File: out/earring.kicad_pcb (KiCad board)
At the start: 4 copper layers, 30.5 x 35.8 mm, 123 parts, among them J1 USB-C, SW1 BOOTSEL, SW2 PWR, U1 RP2350A, U2 LGS4056H, U3 NCP730-3.3, U4 TPS22913, U5 USBLC6-2P6, U6 LSM6DS3TR-C, U7 W25Q16JVUXIQ, Y1 12MHz

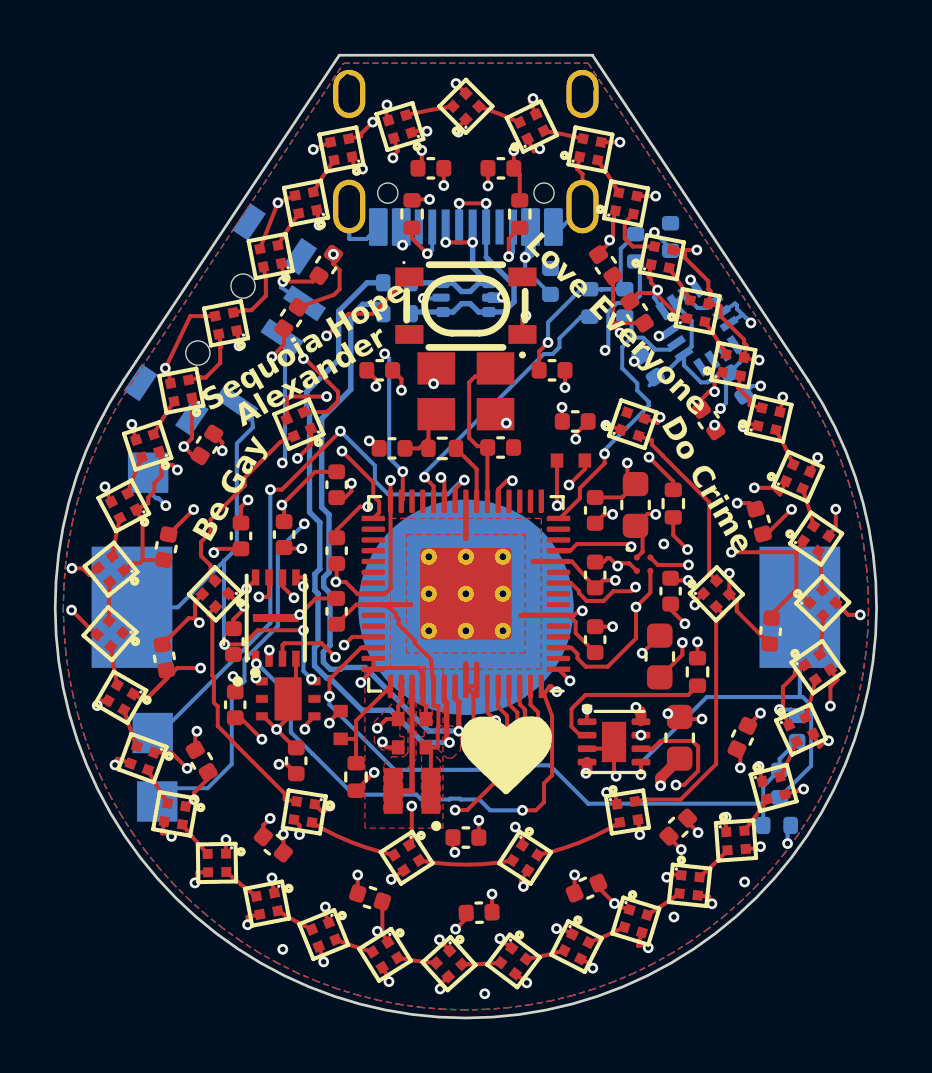
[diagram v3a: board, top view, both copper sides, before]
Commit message: Rev 2 power path: split VBATT from VSYS so USB runs the board
Rev 1 hung the LDO input and the LED load switch on VBATT -- the same
node as the charger's BAT pin -- so the LGS4056H's ~41mA program current
was SHARED with the running system. 17mA of MCU plus 17.5mA of LED rail
left the cell about 6mA, and a flat cell could never climb to the
SK6805-EC10's 3.7V minimum VDD before someone unplugged it. That is the
"no lights at all" failure from Aug 27, and it is a power-path problem,
not a firmware one.

  VBUS  --|>|--  VSYS      D3, B5819WS Schottky, ~0.3V at our ~60mA
  VBATT --[Q2]-- VSYS      CJ2101 P-FET, on only when no cable is in
  VSYS  -> U3 (LDO IN), U4 (LED load switch IN), C18, C29
  VBATT -> U2 pin 5 (charger BAT), BT1, C17, SW2   [cell node ONLY]

Q2's ORIENTATION IS THE WHOLE TRICK: source = VSYS, drain = VBATT. A
P-FET's body diode conducts drain->source, so this way it points
cell->VSYS. It blocks the 4.7V USB rail from back-feeding the cell
around the charger -- which is exactly what the intuitive wiring
(source on the battery) would do through the body diode -- while still
letting the cell carry the load through ~0.4V of diode if VSYS sags
below VBATT, covering the ~200ms of VBUS decay on unplug. Gate is
R22 10k from VBUS against R21 1M to GND: near VBUS with a cable in
(Vgs +0.25V, hard off), and following the dead VBUS node without one.
That node is not floating -- R19/R20 pin it under 0.65V even against
R18's backfeed -- so Vgs is -2.4V at a 3.0V cell and Q2 is fully on.

This retires the R8 22k->15k rework rather than performing it. 22k
already gives 40.9mA, which is exactly the fitted RJD2032C1's rated
40mA charge, and the reason 15k was tempting is gone. The hazard that
blocked it is gone too: with the system off the cell, the full program
current reaches the cell in EITHER switch position.

What else falls out: DONE can finally assert (the cell's current
actually tapers to ITERM now), VBSENSE reads a true unloaded cell while
charging, the r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
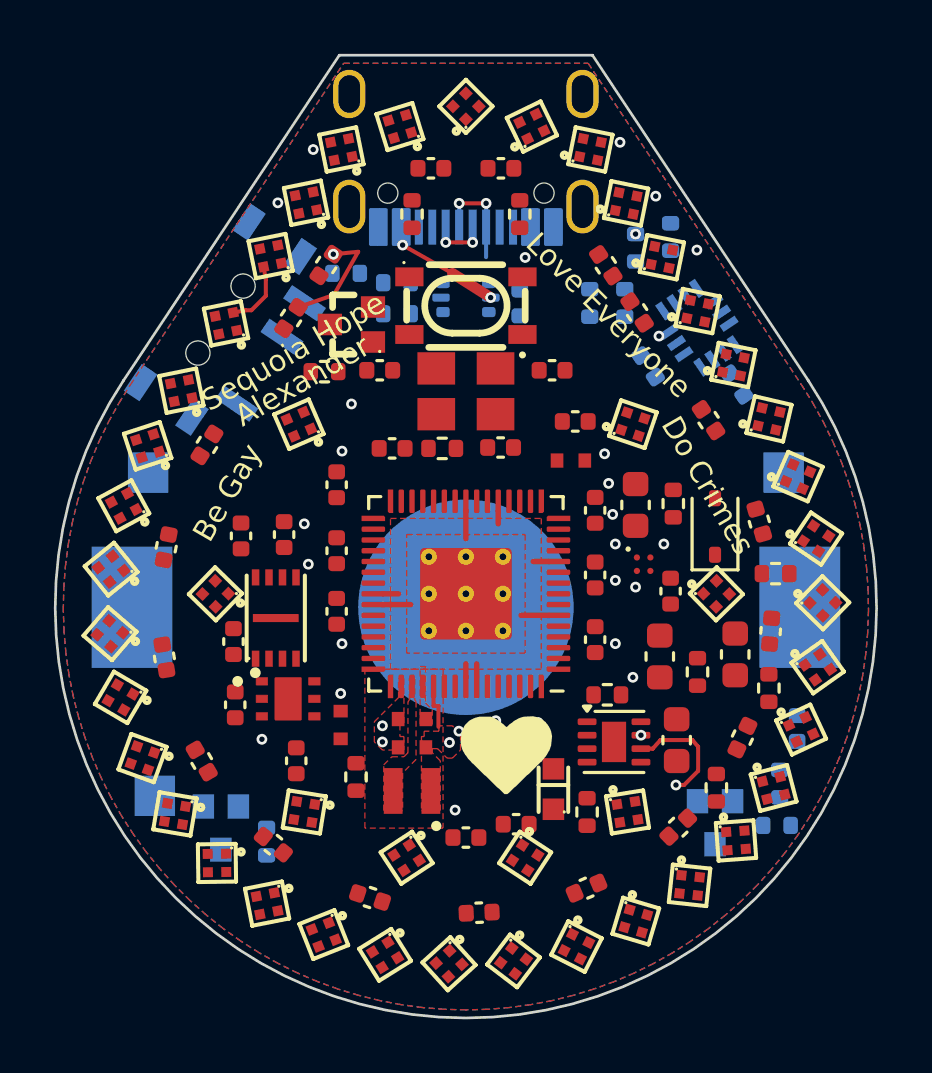
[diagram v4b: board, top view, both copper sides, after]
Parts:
- added C26: 100n, earring:C_0402_1005Metric, F.Cu at (101.9, 108.1)
- added C29: 10u, earring:C_0603_1608Metric, F.Cu at (110.0, 101.8)
- added D2: BAT54S, earring:SOT-323_BAT54SW, B.Cu at (90.9, 108.2)
- added D3: B5819WS, earring:D_SOD-323, F.Cu at (109.2, 97.0)
- added Q1: ALS-PT19, earring:SENSOR_ALS-PT19, F.Cu at (103.2, 106.8)
- added Q2: CJ2101, earring:SOT-323_MOSFET, B.Cu at (109.2, 108.0)
- added Q3: BSS138W, earring:SOT-323_MOSFET, F.Cu at (95.8, 89.5)
- added R16: 22k, earring:R_0402_1005Metric, F.Cu at (104.5, 107.6)
- added R17: 100k, earring:R_0402_1005Metric, B.Cu at (92.6, 108.7)
- added R18: 100k, earring:R_0402_1005Metric, B.Cu at (95.5, 87.6)
- added R19: 10k, earring:R_0402_1005Metric, F.Cu at (105.2, 103.2)
- added R20: 10k, earring:R_0402_1005Metric, F.Cu at (111.5, 98.8)
- added R21: 1M, earring:R_0402_1005Metric, F.Cu at (111.2, 103.0)
- added R22: 10k, earring:R_0402_1005Metric, F.Cu at (109.3, 106.7)
- added R23: 1k, earring:R_0402_1005Metric, F.Cu at (94.8, 91.2)
- moved TP2 25.3 mm to (111.8, 95.0)
- moved C28 1.39 mm to (102.0, 88.7)
- moved TP3 0.23 mm to (88.5, 107.0)
- moved C16 0.14 mm to (107.8, 104.9)
- turned LED33 to 168.563 degrees
- turned LED7 to -61.5215 degrees
- turned C34 to -122.093 degrees
- turned LED31 to 168.563 degrees
- turned LED18 to 52.6709 degrees
- turned LED21 to 83.8143 degrees
- turned LED2 to -78.5634 degrees
- turned C56 to 106.292 degrees
- turned LED29 to 166.863 degrees
- turned LED24 to 114.958 degrees
- turned C32 to -123.563 degrees
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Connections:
- C18 pad 1: VBATT -> VSYS
- J1 pad A8: unconnected-(J1-PadA8) -> (no net)
- J1 pad B8: unconnected-(J1-PadB8) -> (no net)
- LED45 pad 4: unconnected-(LED45-DOUT-Pad4) -> (no net)
- R11 pad 1: VBATT -> SW_ON
- SW2 pad 2: PWR_EN -> SW_ON
- U1 pad 10: unconnected-(U1-GPIO7-Pad10) -> (no net)
- U1 pad 13: unconnected-(U1-GPIO9-Pad13) -> (no net)
- U1 pad 14: unconnected-(U1-GPIO10-Pad14) -> (no net)
- U1 pad 16: unconnected-(U1-GPIO12-Pad16) -> (no net)
- U1 pad 17: unconnected-(U1-GPIO13-Pad17) -> (no net)
- U1 pad 18: unconnected-(U1-GPIO14-Pad18) -> (no net)
- U1 pad 19: unconnected-(U1-GPIO15-Pad19) -> (no net)
- U1 pad 2: unconnected-(U1-GPIO0-Pad2) -> (no net)
- U1 pad 27: unconnected-(U1-GPIO16-Pad27) -> (no net)
- U1 pad 28: unconnected-(U1-GPIO17-Pad28) -> (no net)
- U1 pad 29: LED_D0 -> LED_DATA
- U1 pad 32: unconnected-(U1-GPIO20-Pad32) -> (no net)
- U1 pad 33: unconnected-(U1-GPIO21-Pad33) -> (no net)
- U1 pad 34: unconnected-(U1-GPIO22-Pad34) -> (no net)
- U1 pad 35: unconnected-(U1-GPIO23-Pad35) -> (no net)
- U1 pad 36: unconnected-(U1-GPIO24-Pad36) -> (no net)
- U1 pad 37: unconnected-(U1-GPIO25-Pad37) -> (no net)
- U1 pad 4: unconnected-(U1-GPIO2-Pad4) -> (no net)
- U1 pad 40: unconnected-(U1-GPIO26-Pad40) -> LIGHT
- U1 pad 41: unconnected-(U1-GPIO27-Pad41) -> VBUS_SENSE
- U1 pad 5: unconnected-(U1-GPIO3-Pad5) -> (no net)
- U1 pad 7: unconnected-(U1-GPIO4-Pad7) -> (no net)
- U1 pad 8: unconnected-(U1-GPIO5-Pad8) -> (no net)
- U3 pad 2: unconnected-(U3-GND-Pad2) -> (no net)
- U3 pad 5: unconnected-(U3-OUT-Pad5) -> (no net)
- U3 pad 6: VBATT -> VSYS
- U4 pad A2: VBATT -> VSYS
- U6 pad 10: unconnected-(U6-GND-Pad10) -> (no net)
- U6 pad 11: unconnected-(U6-INT1-Pad11) -> (no net)
- U6 pad 9: unconnected-(U6-GND-Pad9) -> (no net)
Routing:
- net GND: track 114.4 -> 0.00 mm, vias 86 -> 3
- net VLED: track 78.7 -> 4.17 mm, vias 62 -> 6
- net VBATT: track 61.5 -> 0.00 mm, vias 6 -> 0
- net VBUS: track 63.9 -> 3.81 mm, vias 6 -> 3
- net 3V3: track 54.6 -> 2.69 mm, vias 18 -> 8
- net BOOTSEL: track 29.1 -> 0.00 mm, vias 4 -> 0
- net CHRG: track 24.7 -> 0.00 mm
- net USB_DM: track 24.5 -> 0.00 mm
- net VBSENSE: track 24.5 -> 0.00 mm, vias 1 -> 0
- net USB_DP: track 23.3 -> 0.00 mm
- net LED_EN: track 23.2 -> 0.00 mm, vias 3 -> 1
- net RUN: track 22.2 -> 0.00 mm, vias 2 -> 0
- net IMU_SDA: track 21.8 -> 0.00 mm, vias 3 -> 2
- net SWCLK: track 21.6 -> 0.00 mm, vias 3 -> 1
- net SWDIO: track 20.4 -> 0.00 mm, vias 2 -> 1
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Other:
- board text added: "Do Crimes"
- board text removed: "Do Crime"

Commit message: Rev 2 routed: 5 unconnected, 0 DRC errors
First routed board carrying the rev-2 power path. 1371 tracks, 258 vias,
117 warnings (60 silk-over-copper, 40 silk overlap, 6 dangling vias, the
usual crop) and zero errors. NOT orderable -- five nets are still open, so
the fab export was deliberately skipped.

Open:
  VBUS_SENSE  U1.41 -> R19.2   8.2mm cross-board
  LIGHT       U1.40 -> Q1.2    7.3mm cross-board
  VBUS        x2: the tip trunk (the 3 segs route.py reported blocked by
              routed copper) and the short branch to the new R19
  3V3         a 1.6mm stub at the MCU

The two long ones share a cause. Both leave the MCU's jammed west pin
window -- pins 40 and 41, at radius 3.45 and 3.51mm -- and have to reach
the east side. The B.Cu hop straight across is not available: BT1 sits on
the back with a 8mm GND pad dead centre, so the back inside r4.0 is solid
copper and a via wants r > 4.4. Both nets originate INSIDE that disc and
have to escape radially on F.Cu past the coin before the back layer
exists for them at all, which is why the one-committed-B-transition-via
trick that works for this board's other stranded nets does not apply.

Six attempts, one real sample:

  attempt 1   route 19 -> finish  5   <- best, kept
  attempt 2   route 30 -> finish 14
  attempt 3   route 30 -> finish 13
  attempt 4   route 30 -> finish 14
  attempt 5   route 30 -> finish 14
  attempt 6   route 30 -> finish 14

Attempts 2-6 routed to exactly 30 every time. That is not seed variance,
and build.py's retry unit is built on the assumption that it is
("freerouting is seed-dependent, so a failed finish re-rolls the
routing"). The one thing that made attempt 1 different is that it started
from a board that had never been through a completed route -- the earlier
run hung inside freerouting, so it left pre-routes and zones but no
post-route pours, keepouts or ring stubs -- while 2-6 each started from
the previous attempt's finished board. wipe() does delete every track and
zone, so t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
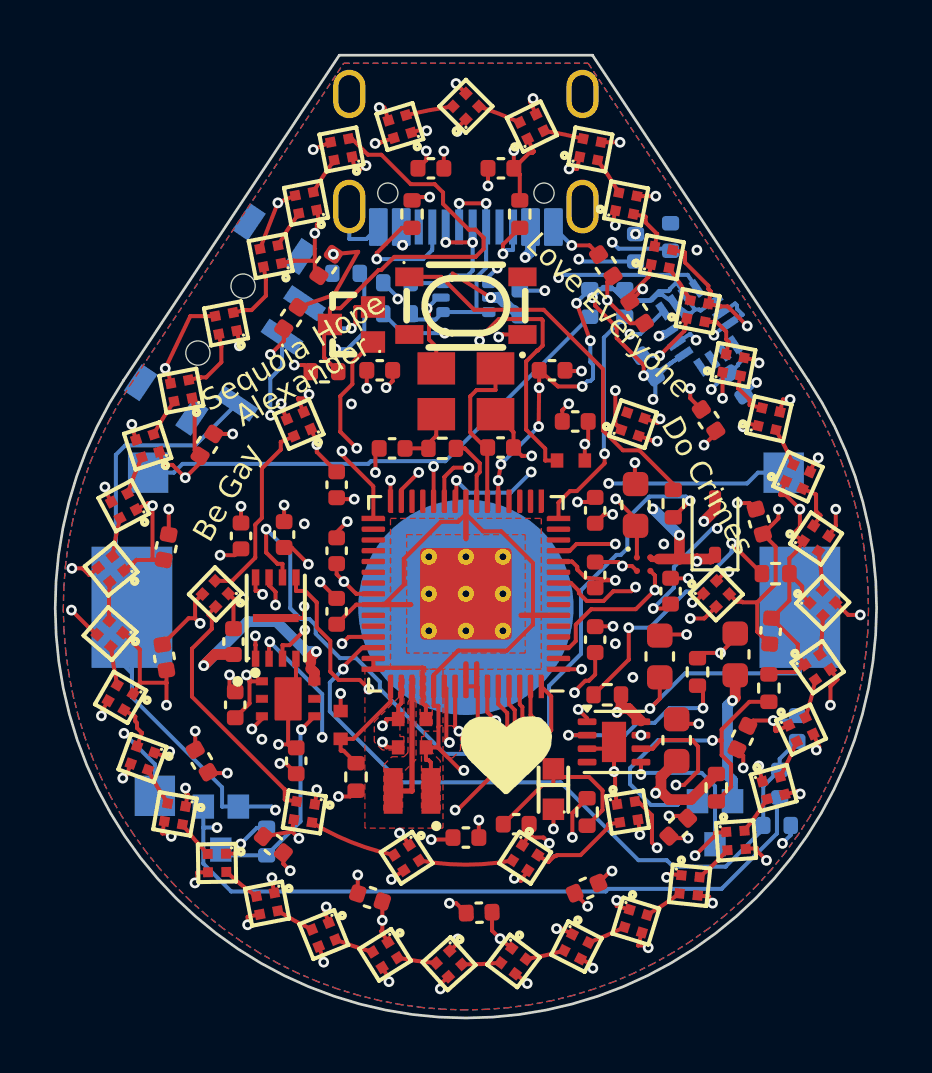
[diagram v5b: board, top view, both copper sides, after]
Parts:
- turned LED33 to 169 degrees
- turned LED7 to -62 degrees
- turned C34 to -122 degrees
- turned LED31 to 169 degrees
- turned LED18 to 53 degrees
- turned LED21 to 84 degrees
- turned LED2 to -79 degrees
- turned C56 to 106 degrees
- turned LED29 to 167 degrees
- turned LED24 to 115 degrees
- turned C32 to -124 degrees
- turned LED3 to -79 degrees
- turned LED26 to 136 degrees
- turned C40 to -60 degrees
- turned LED14 to 11 degrees
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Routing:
- net GND: track 0.00 -> 135.3 mm, vias 3 -> 83
- net VLED: track 4.17 -> 83.6 mm, vias 6 -> 63
- net 3V3: track 2.69 -> 64.6 mm, vias 8 -> 30
- net VBATT: track 0.00 -> 56.9 mm, vias 0 -> 3
- net VDD_CORE: track 4.46 -> 59.3 mm, vias 0 -> 3
- net VBUS: track 3.81 -> 52.6 mm, vias 3 -> 6
- net SW_ON: track 0.00 -> 46.1 mm, vias 0 -> 2
- net VSYS: track 0.00 -> 38.2 mm, vias 0 -> 6
- net BOOTSEL: track 0.00 -> 30.9 mm, vias 0 -> 3
- net CHRG: track 0.00 -> 26.5 mm
- net VBSENSE: track 0.00 -> 26.1 mm, vias 0 -> 1
- net PWR_EN: track 0.00 -> 25.9 mm, vias 0 -> 2
- net SWDIO: track 0.00 -> 22.7 mm, vias 1 -> 3
- net LED_EN: track 0.00 -> 22.2 mm, vias 1 -> 3
- net RUN: track 0.00 -> 20.3 mm, vias 0 -> 1
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
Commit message: Rev 2 coin-cell close-out: name the clip not the cell, BS-6 socket fit test
BT1's value is now the clip's MPN (MY-2032-12-R) so the BOM Comment agrees
with its LCSC column; design.yaml's power.battery is the one place the
hand-fitted RJD2032C1 cell is named. Adds the C22363833 (CR2032-BS-6) fit
study (scripts/gen_bs6_svg.py + dashboard entry): its land runs 1.19mm off
the board, and the only land-legal rotations put the body on J1.

Last commit of the coin-cell power source before the LiPo change.

Co-Authored-By: Claude Opus 5.5 <noreply@anthropic.com>
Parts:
- BT1: value LIR2032 -> MY-2032-12-R
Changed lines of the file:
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@@
 		(at 100 100 180)
 		(descr "MYOUNG MY-2032-12-R SMD coin cell retainer clip, LCSC C964834. Clip=+ (pin1), center pad=- (pin2). Flat feet, no thru-holes. Copper identical to BAT_CR2032_W (ordered rev).")
-		(tags "battery LIR2032 CR2032 retainer")
+		(tags "battery RJD2032C1 CR2032 retainer")
 		(property "Reference" "BT1"
 			(at 0 13.2 0)
@@
 			)
 		)
-		(property "Value" "LIR2032"
+		(property "Value" "MY-2032-12-R"
 			(at 0 -13.2 0)
 			(layer "B.Fab")
